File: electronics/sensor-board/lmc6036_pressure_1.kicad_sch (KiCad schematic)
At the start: 10 parts, among them U12 LMC6036, U16 LMC6036

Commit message: work on sensor-board
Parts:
- removed U12, U16: LMC6036, LMC6036:SOP65P640X120-14N, symbol LMC6036_custom:LMC6036
- added U13: LMC6036, LMC6036:SOP65P640X120-14N, symbol LMC6036_custom:LMC6036
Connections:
- net VDD: now also U13.4 (VDD)
- net VSS: now also U13.11 (VSS)
- net output_A: now also U13.1 (OUTA), U13.2 (INA-)
- net output_B: now also U13.6 (INB-), U13.7 (OUTB)
- net output_C: now also U13.8 (OUTC), U13.9 (INC-)
- net output_D: now also U13.13 (IND-), U13.14 (OUTD)
- net at R82.1, R86.1: now also U13.3 (INA+)
- net at R83.1, R87.1: now also U13.5 (INB+)
- net at R85.1, R89.1: now also U13.12 (IND+)
- net at R84.1, R88.1: now also U13.10 (INC+)
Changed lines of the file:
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@@
   (junction (at 142.24 120.65) (diameter 0) (color 0 0 0 0))
   (junction (at 142.24 148.59) (diameter 0) (color 0 0 0 0))
-  (junction (at 162.56 63.5) (diameter 0) (color 0 0 0 0))
-  (junction (at 162.56 90.17) (diameter 0) (color 0 0 0 0))
-  (junction (at 162.56 118.11) (diameter 0) (color 0 0 0 0))
-  (junction (at 162.56 146.05) (diameter 0) (color 0 0 0 0))
   (wire (pts (xy 125.73 60.96) (xy 135.89 60.96))
     (stroke (width 0) (type default) (color 0 0 0 0))
@@
   (symbol (lib_id "LMC6036_custom:LMC6036") (at 153.67 44.45 90) (unit 5)
     (in_bom yes) (on_board yes) (fields_autoplaced)
-    (property "Reference" "U12" (id 0) (at 153.67 35.56 90))
+    (property "Reference" "U13" (id 0) (at 153.67 35.56 90))
     (property "Value" "LMC6036" (id 1) (at 153.67 38.1 90))
     (property "Footprint" "LMC6036:SOP65P640X120-14N" (id 2) (at 153.67 42.545 0)
@@
   )
   (symbol (lib_id "LMC6036_custom:LMC6036") (at 153.67 63.5 0) (unit 1)
-    (in_bom yes) (on_board yes)
-    (property "Reference" "U16" (id 0) (at 154.94 53.34 0))
-    (property "Value" "LMC6036" (id 1) (at 160.02 68.58 0))
+    (in_bom yes) (on_board yes) (fields_autoplaced)
+    (property "Reference" "U13" (id 0) (at 154.94 53.34 0))
+    (property "Value" "LMC6036" (id 1) (at 154.94 55.88 0))
     (property "Footprint" "LMC6036:SOP65P640X120-14N" (id 2) (at 155.575 63.5 0)
       (effects (font (size 1.27 1.27)) hide)
@@
   (symbol (lib_id "LMC6036_custom:LMC6036") (at 153.67 90.17 0) (unit 2)
     (in_bom yes) (on_board yes) (fields_autoplaced)
-    (property "Reference" "U12" (id 0) (at 154.94 80.01 0))
+    (property "Reference" "U13" (id 0) (at 154.94 80.01 0))
     (property "Value" "LMC6036" (id 1) (at 154.94 82.55 0))
     (property "Footprint" "LMC6036:SOP65P640X120-14N" (id 2) (at 155.575 90.17 0)
@@
   (symbol (lib_id "LMC6036_custom:LMC6036") (at 153.67 118.11 0) (unit 3)
     (in_bom yes) (on_board yes) (fields_autoplaced)
-    (property "Reference" "U12" (id 0) (at 154.94 107.95 0))
+    (property "Reference" "U13" (id 0) (at 154.94 107.95 0))
     (property "Value" "LMC6036" (id 1) (at 154.94 110.49 0))
     (property "Footprint" "LMC6036:SOP65P640X120-14N" (id 2) (at 155.575 118.11 0)
@@
   (symbol (lib_id "LMC6036_custom:LMC6036") (at 153.67 146.05 0) (unit 4)
     (in_bom yes) (on_board yes) (fields_autoplaced)
-    (property "Reference" "U12" (id 0) (at 154.94 135.89 0))
+    (property "Reference" "U13" (id 0) (at 154.94 135.89 0))
     (property "Value" "LMC6036" (id 1) (at 154.94 138.43 0))
     (property "Footprint" "LMC6036:SOP65P640X120-14N" (id 2) (at 155.575 146.05 0)

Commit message: More work on sensor-board
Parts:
- R82, R83, R84, R85, R86, R87, R88, R89: value 150 -> 100
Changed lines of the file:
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@@
     (in_bom yes) (on_board yes) (fields_autoplaced)
     (property "Reference" "R82" (id 0) (at 135.89 59.69 90))
-    (property "Value" "150" (id 1) (at 135.89 62.23 90))
+    (property "Value" "100" (id 1) (at 135.89 62.23 90))
     (property "Footprint" "Resistor_SMD:R_0603_1608Metric" (id 2) (at 135.89 64.262 90)
       (effects (font (size 1.27 1.27)) hide)
@@
     (in_bom yes) (on_board yes) (fields_autoplaced)
     (property "Reference" "R83" (id 0) (at 135.89 86.36 90))
-    (property "Value" "150" (id 1) (at 135.89 88.9 90))
+    (property "Value" "100" (id 1) (at 135.89 88.9 90))
     (property "Footprint" "Resistor_SMD:R_0603_1608Metric" (id 2) (at 135.89 90.932 90)
       (effects (font (size 1.27 1.27)) hide)
@@
       (effects (font (size 1.27 1.27)) (justify left))
     )
-    (property "Value" "150" (id 1) (at 144.78 126.9999 0)
+    (property "Value" "100" (id 1) (at 144.78 126.9999 0)
       (effects (font (size 1.27 1.27)) (justify left))
     )
@@
     (in_bom yes) (on_board yes) (fields_autoplaced)
     (property "Reference" "R84" (id 0) (at 135.89 114.3 90))
-    (property "Value" "150" (id 1) (at 135.89 116.84 90))
+    (property "Value" "100" (id 1) (at 135.89 116.84 90))
     (property "Footprint" "Resistor_SMD:R_0603_1608Metric" (id 2) (at 135.89 118.872 90)
       (effects (font (size 1.27 1.27)) hide)
@@
       (effects (font (size 1.27 1.27)) (justify left))
     )
-    (property "Value" "150" (id 1) (at 144.78 154.9399 0)
+    (property "Value" "100" (id 1) (at 144.78 154.9399 0)
       (effects (font (size 1.27 1.27)) (justify left))
     )
@@
       (effects (font (size 1.27 1.27)) (justify left))
     )
-    (property "Value" "150" (id 1) (at 144.78 72.3899 0)
+    (property "Value" "100" (id 1) (at 144.78 72.3899 0)
       (effects (font (size 1.27 1.27)) (justify left))
     )
@@
     (in_bom yes) (on_board yes) (fields_autoplaced)
     (property "Reference" "R85" (id 0) (at 135.89 142.24 90))
-    (property "Value" "150" (id 1) (at 135.89 144.78 90))
+    (property "Value" "100" (id 1) (at 135.89 144.78 90))
     (property "Footprint" "Resistor_SMD:R_0603_1608Metric" (id 2) (at 135.89 146.812 90)
       (effects (font (size 1.27 1.27)) hide)
@@
       (effects (font (size 1.27 1.27)) (justify left))
     )
-    (property "Value" "150" (id 1) (at 144.78 99.0599 0)
-      (effects (font (size 1.27 1.27)) (justify left))
-    )
+    (property "Value" "100" (id 1) (at 144.78 99.0599 0)
+      (effects (font (size 1.27 1.27)) (justify left))
+    )

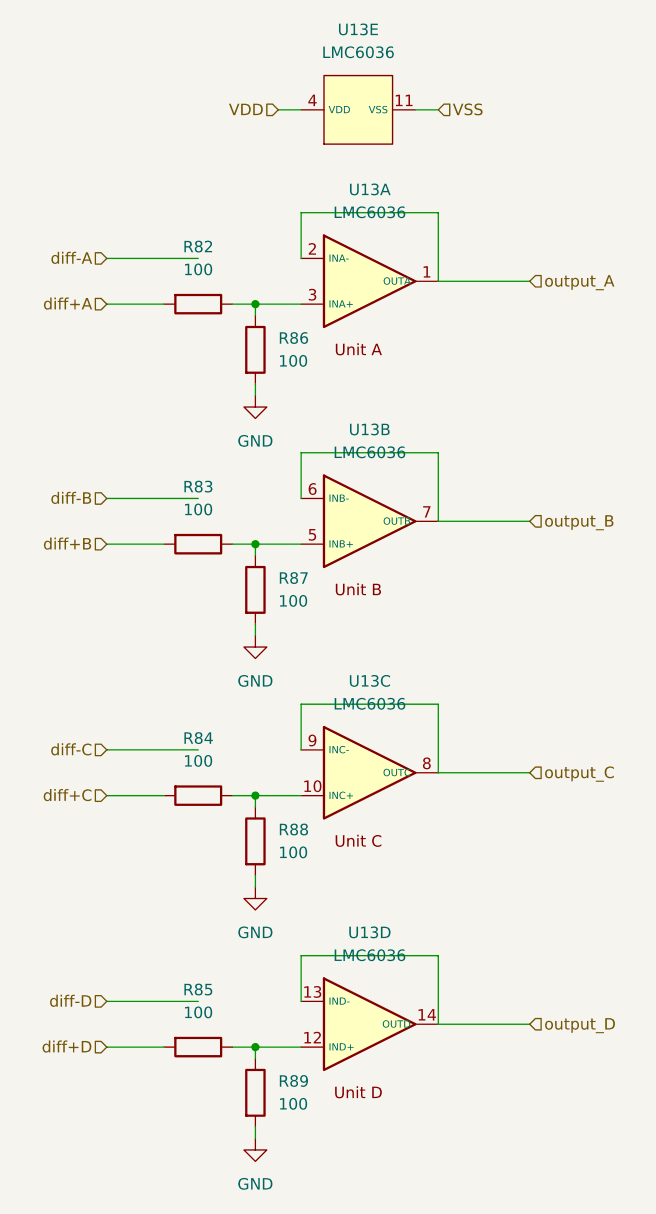
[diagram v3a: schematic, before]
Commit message: updated loadcell amplifier
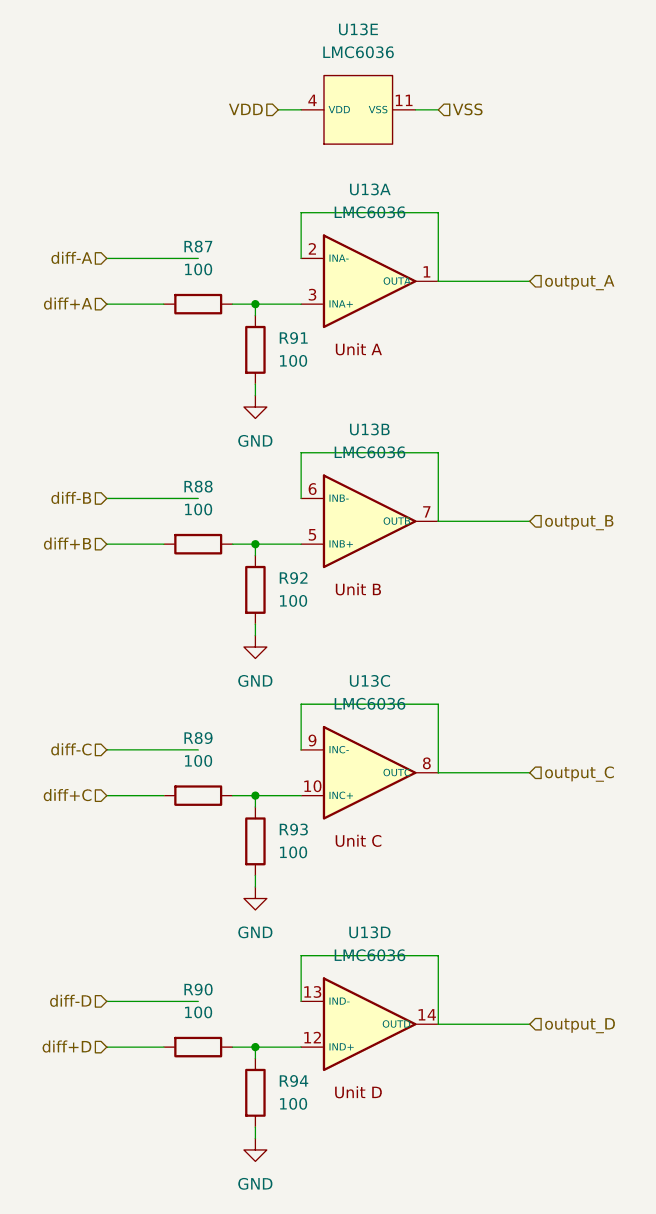
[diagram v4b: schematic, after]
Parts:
- renumbered R82 to R87, R83 to R88, R84 to R89, R85 to R90, R86 to R91, R87 to R92, R88 to R93, R89 to R94
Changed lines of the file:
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@@
   (symbol (lib_id "Device:R") (at 135.89 66.04 270) (unit 1)
     (in_bom yes) (on_board yes) (fields_autoplaced)
-    (property "Reference" "R82" (id 0) (at 135.89 59.69 90))
+    (property "Reference" "R87" (id 0) (at 135.89 59.69 90))
     (property "Value" "100" (id 1) (at 135.89 62.23 90))
     (property "Footprint" "Resistor_SMD:R_0603_1608Metric" (id 2) (at 135.89 64.262 90)
@@
   (symbol (lib_id "Device:R") (at 135.89 92.71 270) (unit 1)
     (in_bom yes) (on_board yes) (fields_autoplaced)
-    (property "Reference" "R83" (id 0) (at 135.89 86.36 90))
+    (property "Reference" "R88" (id 0) (at 135.89 86.36 90))
     (property "Value" "100" (id 1) (at 135.89 88.9 90))
     (property "Footprint" "Resistor_SMD:R_0603_1608Metric" (id 2) (at 135.89 90.932 90)
@@
   (symbol (lib_id "power:GND") (at 142.24 76.2 0) (unit 1)
     (in_bom yes) (on_board yes) (fields_autoplaced)
-    (property "Reference" "#PWR0123" (id 0) (at 142.24 82.55 0)
+    (property "Reference" "#PWR0138" (id 0) (at 142.24 82.55 0)
       (effects (font (size 1.27 1.27)) hide)
     )
@@
   (symbol (lib_id "Device:R") (at 142.24 125.73 0) (unit 1)
     (in_bom yes) (on_board yes) (fields_autoplaced)
-    (property "Reference" "R88" (id 0) (at 144.78 124.4599 0)
+    (property "Reference" "R93" (id 0) (at 144.78 124.4599 0)
       (effects (font (size 1.27 1.27)) (justify left))
     )
@@
   (symbol (lib_id "Device:R") (at 135.89 120.65 270) (unit 1)
     (in_bom yes) (on_board yes) (fields_autoplaced)
-    (property "Reference" "R84" (id 0) (at 135.89 114.3 90))
+    (property "Reference" "R89" (id 0) (at 135.89 114.3 90))
     (property "Value" "100" (id 1) (at 135.89 116.84 90))
     (property "Footprint" "Resistor_SMD:R_0603_1608Metric" (id 2) (at 135.89 118.872 90)
@@
   (symbol (lib_id "Device:R") (at 142.24 153.67 0) (unit 1)
     (in_bom yes) (on_board yes) (fields_autoplaced)
-    (property "Reference" "R89" (id 0) (at 144.78 152.3999 0)
+    (property "Reference" "R94" (id 0) (at 144.78 152.3999 0)
       (effects (font (size 1.27 1.27)) (justify left))
     )
@@
   (symbol (lib_id "Device:R") (at 142.24 71.12 0) (unit 1)
     (in_bom yes) (on_board yes) (fields_autoplaced)
-    (property "Reference" "R86" (id 0) (at 144.78 69.8499 0)
+    (property "Reference" "R91" (id 0) (at 144.78 69.8499 0)
       (effects (font (size 1.27 1.27)) (justify left))
     )
@@
   (symbol (lib_id "Device:R") (at 135.89 148.59 270) (unit 1)
     (in_bom yes) (on_board yes) (fields_autoplaced)
-    (property "Reference" "R85" (id 0) (at 135.89 142.24 90))
+    (property "Reference" "R90" (id 0) (at 135.89 142.24 90))
     (property "Value" "100" (id 1) (at 135.89 144.78 90))
     (property "Footprint" "Resistor_SMD:R_0603_1608Metric" (id 2) (at 135.89 146.812 90)
@@
   (symbol (lib_id "power:GND") (at 142.24 158.75 0) (unit 1)
     (in_bom yes) (on_board yes) (fields_autoplaced)
-    (property "Reference" "#PWR0126" (id 0) (at 142.24 165.1 0)
+    (property "Reference" "#PWR0141" (id 0) (at 142.24 165.1 0)
       (effects (font (size 1.27 1.27)) hide)
     )
@@
   (symbol (lib_id "power:GND") (at 142.24 130.81 0) (unit 1)
     (in_bom yes) (on_board yes) (fields_autoplaced)
-    (property "Reference" "#PWR0125" (id 0) (at 142.24 137.16 0)
+    (property "Reference" "#PWR0140" (id 0) (at 142.24 137.16 0)
       (effects (font (size 1.27 1.27)) hide)
     )
@@
   (symbol (lib_id "power:GND") (at 142.24 102.87 0) (unit 1)
     (in_bom yes) (on_board yes) (fields_autoplaced)
-    (property "Reference" "#PWR0124" (id 0) (at 142.24 109.22 0)
+    (property "Reference" "#PWR0139" (id 0) (at 142.24 109.22 0)
       (effects (font (size 1.27 1.27)) hide)
     )
@@
   (symbol (lib_id "Device:R") (at 142.24 97.79 0) (unit 1)
     (in_bom yes) (on_board yes) (fields_autoplaced)
-    (property "Reference" "R87" (id 0) (at 144.78 96.5199 0)
-      (effects (font (size 1.27 1.27)) (justify left))
-    )
+    (property "Reference" "R92" (id 0) (at 144.78 96.5199 0)
+      (effects (font (size 1.27 1.27)) (justify left))
+    )
